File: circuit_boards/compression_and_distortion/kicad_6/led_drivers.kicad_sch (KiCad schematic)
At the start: 5 parts, among them U6 TL072

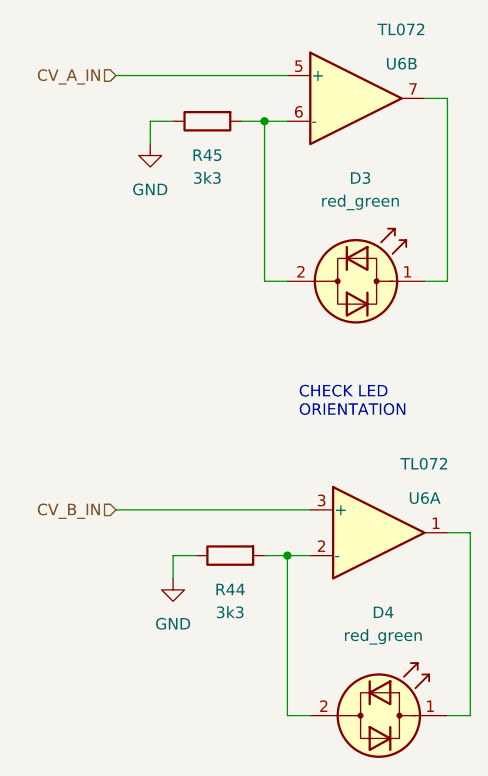
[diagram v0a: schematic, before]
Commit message: Fix a/b swap error and dim LED error
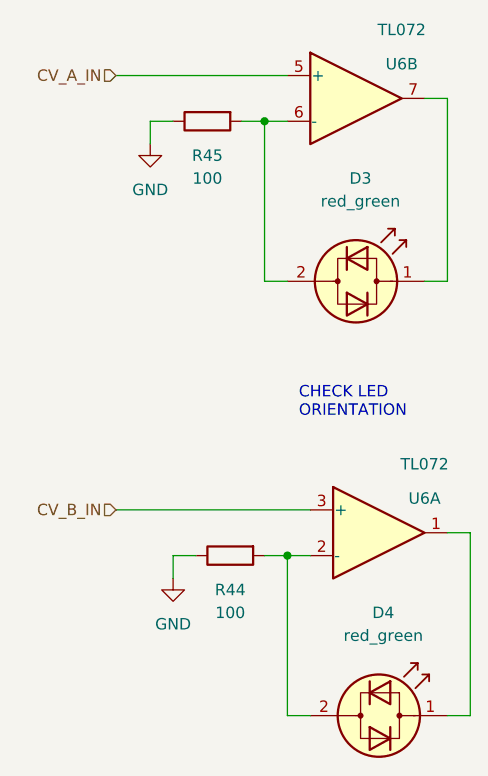
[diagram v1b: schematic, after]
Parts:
- R44, R45: value 3k3 -> 100
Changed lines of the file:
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@@
   (title_block
     (title "M.S.M. Stereo Lowpass Filter Pedal")
-    (date "2022-05-26")
-    (rev "0")
+    (date "2023-04-15")
+    (rev "0.1")
     (comment 2 "creativecommons.org/licenses/by/4.0")
     (comment 3 "License: CC by 4.0")
@@
     (in_bom yes) (on_board yes)
     (property "Reference" "R45" (id 0) (at 142.24 78.74 90))
-    (property "Value" "3k3" (id 1) (at 142.24 81.28 90))
+    (property "Value" "100" (id 1) (at 142.24 81.28 90))
     (property "Footprint" "Resistor_SMD:R_0805_2012Metric" (id 2) (at 142.24 73.152 90)
       (effects (font (size 1.27 1.27)) hide)
@@
     (in_bom yes) (on_board yes)
     (property "Reference" "R44" (id 0) (at 144.78 127 90))
-    (property "Value" "3k3" (id 1) (at 144.78 129.54 90))
+    (property "Value" "100" (id 1) (at 144.78 129.54 90))
     (property "Footprint" "Resistor_SMD:R_0805_2012Metric" (id 2) (at 144.78 121.412 90)
       (effects (font (size 1.27 1.27)) hide)
